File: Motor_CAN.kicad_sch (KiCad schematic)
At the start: 18 parts, among them J19 CAN_OUT, J20 MotorCANConnector, J27 CAN_TP, U14 ADM3055E, U15 CDSOT23-T24CAN

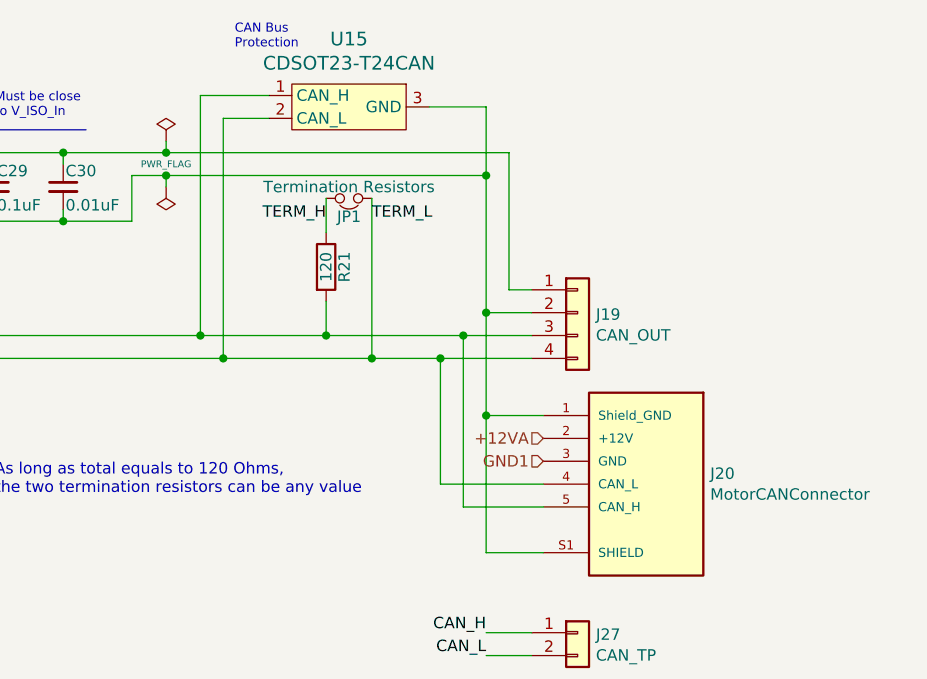
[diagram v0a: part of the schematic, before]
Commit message: Remove 12V isolator, swap CAN connector pins, etc.
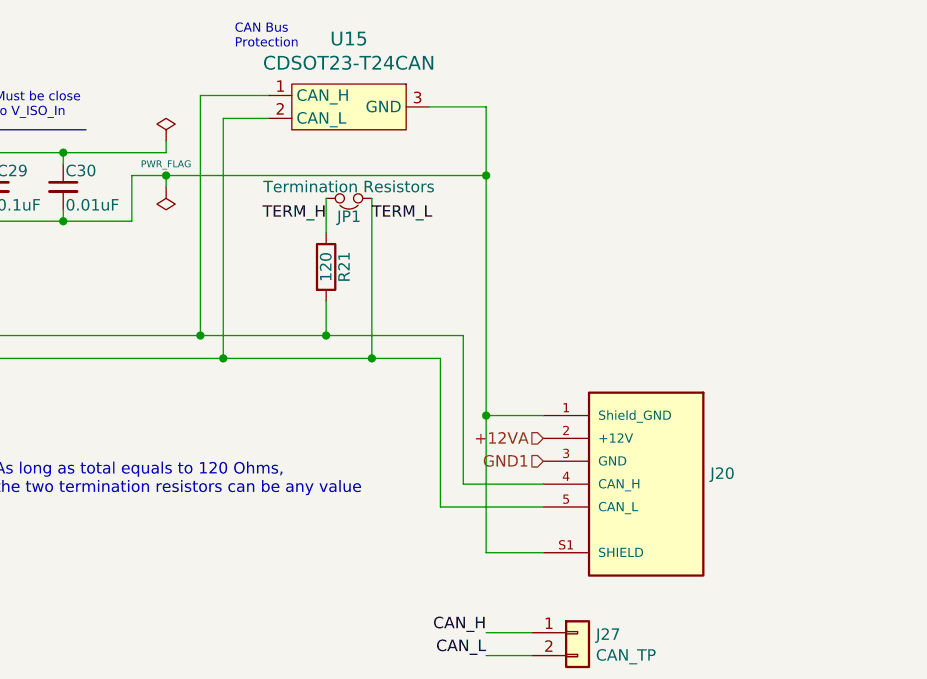
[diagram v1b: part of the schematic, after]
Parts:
- removed J19: CAN_OUT, UTSVT_Connectors:Molex_MicroFit3.0_1x4xP3.00mm_PolarizingPeg_Vertical, symbol Connector_Generic:Conn_01x04
- J20: value MotorCANConnector -> (none); symbol Dashboard-rescue:MotorCANConnector-utsvt-connectors -> Dashboard:MotorCANConnector-utsvt-connectors
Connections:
- net CAN_H: now also J20.4 (CAN_H); no longer J20.5 (CAN_H)
- net CAN_L: now also J20.5 (CAN_L); no longer J20.4 (CAN_L)

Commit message: Release v2.4 and gerbers
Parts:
- J20: value (none) -> MotorCANConnector
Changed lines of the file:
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@@
       (effects (font (size 1.27 1.27)) (justify right))
     )
-    (property "Value" "" (id 1) (at 244.602 119.253 0)
+    (property "Value" "MotorCANConnector" (id 1) (at 244.602 119.253 0)
       (effects (font (size 1.27 1.27)) (justify right))
     )

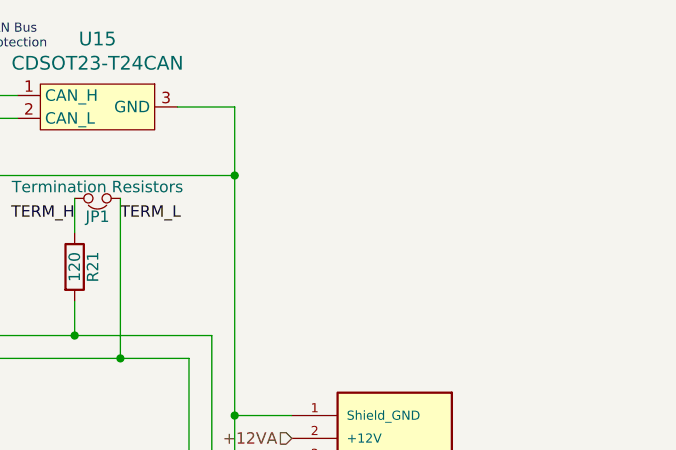
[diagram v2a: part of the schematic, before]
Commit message: Schematic notations for rework changes
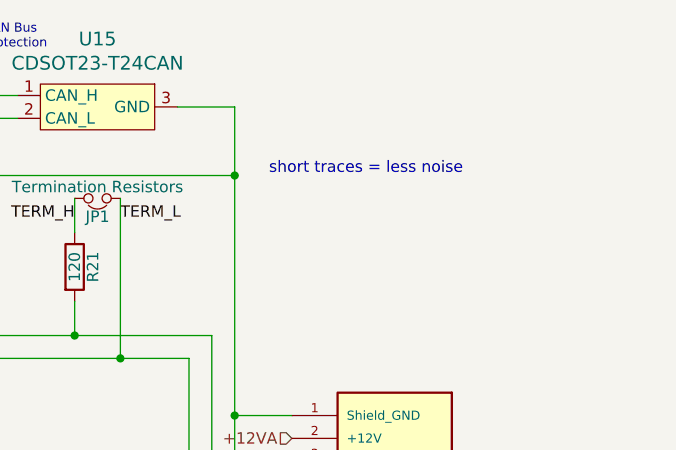
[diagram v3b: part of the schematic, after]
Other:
- note added: "short traces = less noise"

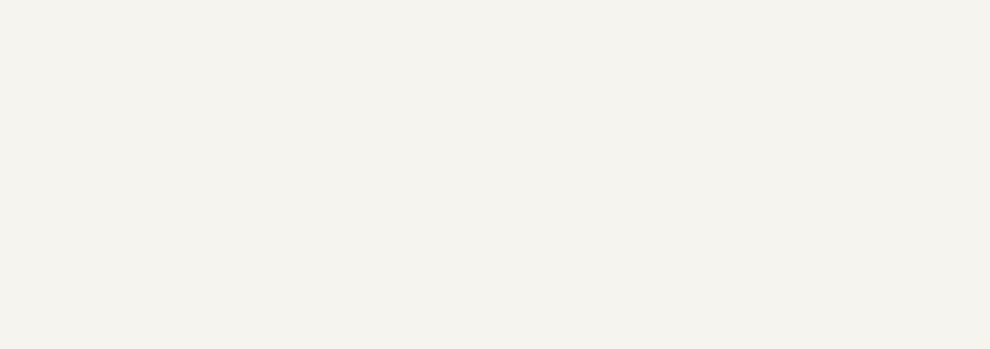
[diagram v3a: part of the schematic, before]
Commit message: Updated schematic in accordance to previous weeks annotated changes
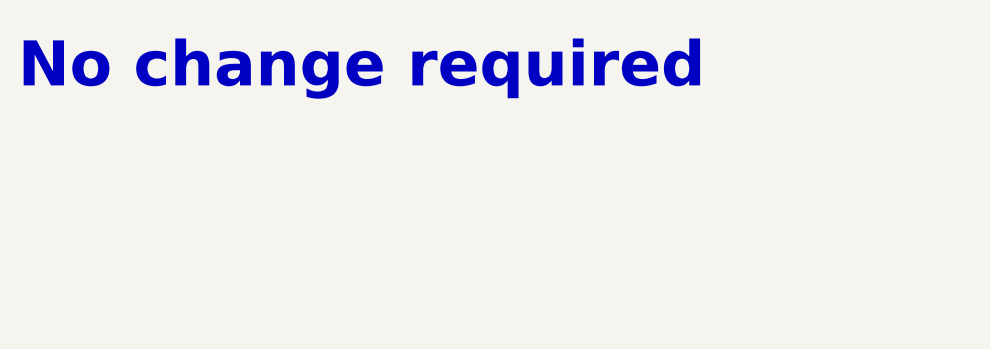
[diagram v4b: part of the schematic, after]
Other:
- note added: "No change required"
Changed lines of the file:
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@@
     (effects (font (size 1.27 1.27)) (justify left bottom))
+  )
+  (text "No change required\n" (at 15.24 22.86 0)
+    (effects (font (face "KiCad Font") (size 5 5) (thickness 1) bold (color 255 2 13 1)) (justify left bottom))
   )
   (text "CAN Bus\nProtection" (at 191.77 69.85 0)

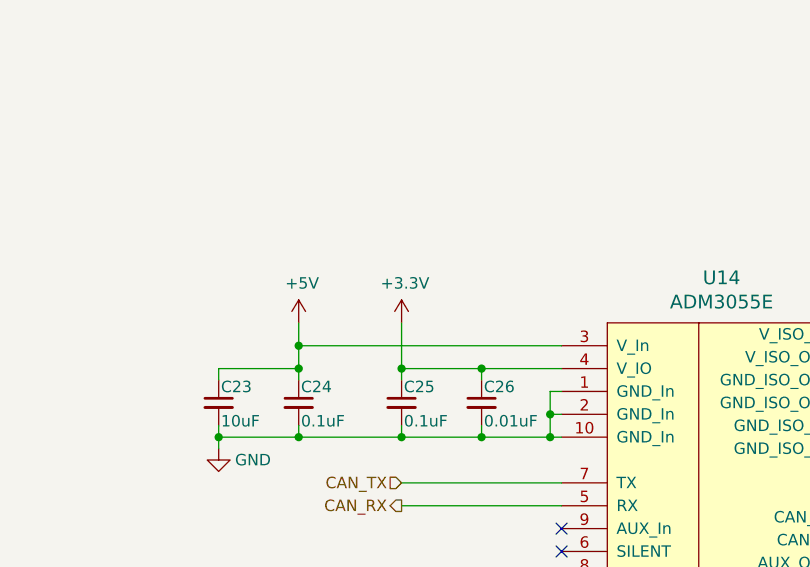
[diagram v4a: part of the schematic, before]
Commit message: Renamed Clk to PA5, removed CAN_TX/RX test points, deleted other .lck file and #auto_saved_files# (hopefully this does not break anything.
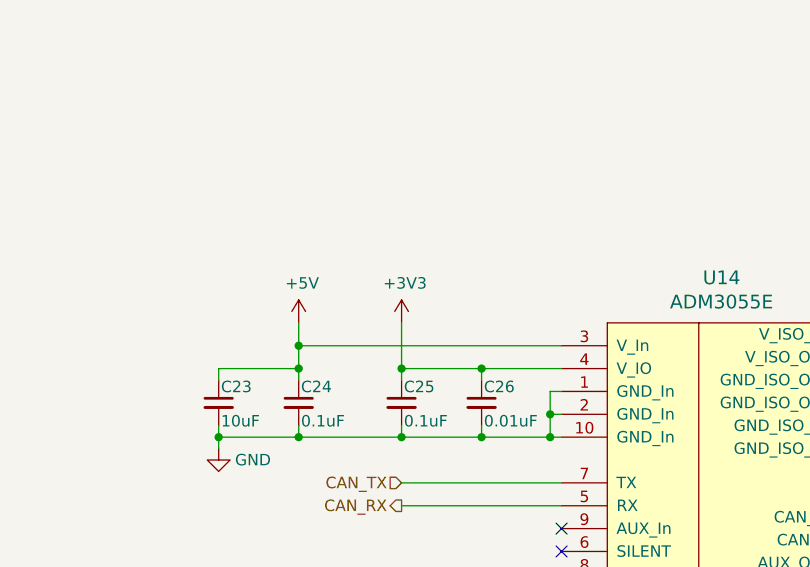
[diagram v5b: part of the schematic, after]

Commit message: Schematic finished :) hopefully not broken
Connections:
- net +12VA renamed +12V
- net GND1 renamed GNDPWR
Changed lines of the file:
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@@
 		)
 	)
-	(hierarchical_label "+12VA"
+	(hierarchical_label "+12V"
 		(shape input)
 		(at 226.06 113.03 180)
@@
 		)
 	)
-	(hierarchical_label "GND1"
+	(hierarchical_label "GNDPWR"
 		(shape input)
 		(at 226.06 115.57 180)

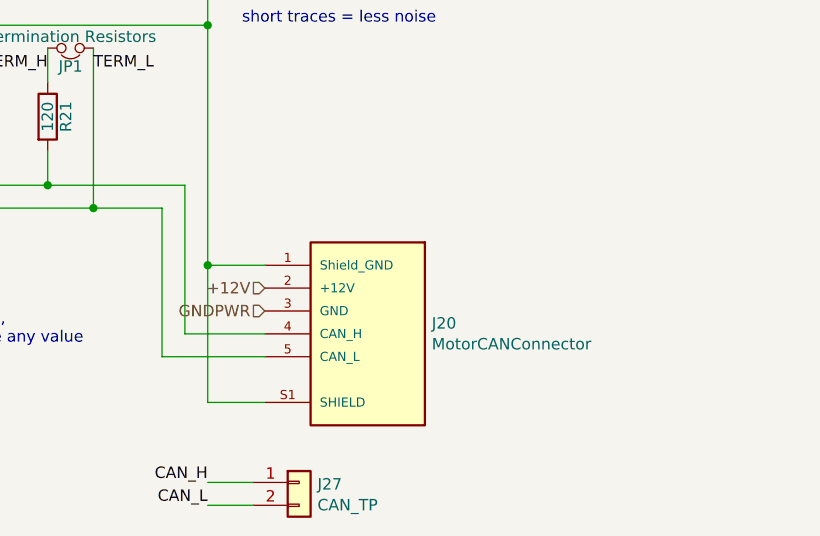
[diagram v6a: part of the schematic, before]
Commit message: Fuse added for motorCAN 12V
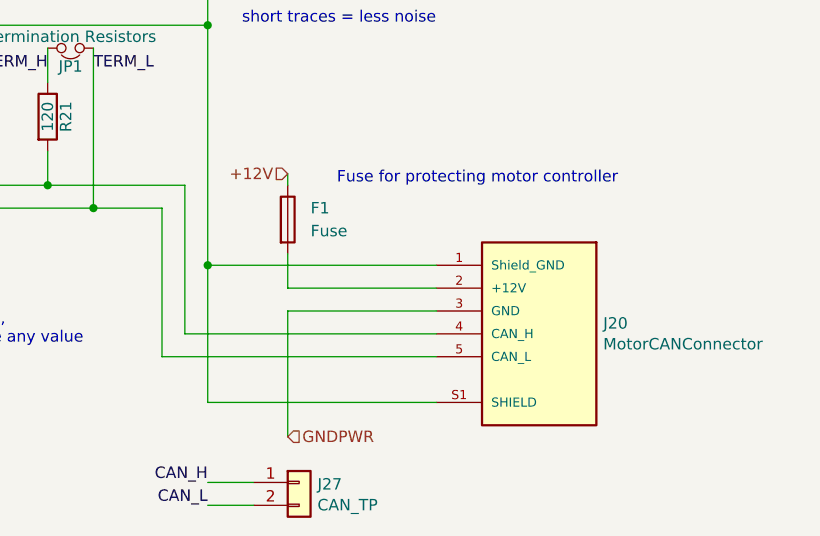
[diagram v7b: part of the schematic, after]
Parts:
- added F1: Fuse, symbol Device:Fuse
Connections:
- net +12V: now also F1.1; no longer J20.2 (+12V)
- new net: F1.2, J20.2 (+12V)
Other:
- note added: "Fuse for protecting motor controller"
- moved on the sheet: J20
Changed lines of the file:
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@@
 	(wire
 		(pts
-			(xy 219.71 110.49) (xy 226.06 110.49)
+			(xy 228.6 115.57) (xy 245.11 115.57)
+		)
+		(stroke
+			(width 0)
+			(type default)
+		)
+	)
+	(wire
+		(pts
+			(xy 219.71 110.49) (xy 245.11 110.49)
 		)
 		(stroke
@@
 	(wire
 		(pts
-			(xy 219.71 125.73) (xy 226.06 125.73)
+			(xy 219.71 125.73) (xy 245.11 125.73)
 		)
 		(stroke
@@
 	(wire
 		(pts
+			(xy 228.6 109.22) (xy 228.6 113.03)
+		)
+		(stroke
+			(width 0)
+			(type default)
+		)
+	)
+	(wire
+		(pts
 			(xy 187.96 74.93) (xy 187.96 101.6)
 		)
@@
 	(wire
 		(pts
-			(xy 217.17 118.11) (xy 226.06 118.11)
+			(xy 217.17 118.11) (xy 245.11 118.11)
 		)
 		(stroke
@@
 	(wire
 		(pts
+			(xy 228.6 101.6) (xy 228.6 100.33)
+		)
+		(stroke
+			(width 0)
+			(type default)
+		)
+	)
+	(wire
+		(pts
 			(xy 53.34 85.09) (xy 62.23 85.09)
 		)
@@
 	(wire
 		(pts
+			(xy 228.6 129.54) (xy 228.6 115.57)
+		)
+		(stroke
+			(width 0)
+			(type default)
+		)
+	)
+	(wire
+		(pts
 			(xy 195.58 74.93) (xy 187.96 74.93)
 		)
@@
 	(wire
 		(pts
+			(xy 228.6 113.03) (xy 245.11 113.03)
+		)
+		(stroke
+			(width 0)
+			(type default)
+		)
+	)
+	(wire
+		(pts
 			(xy 219.71 110.49) (xy 219.71 125.73)
 		)
@@
 	(wire
 		(pts
-			(xy 214.63 120.65) (xy 226.06 120.65)
+			(xy 214.63 120.65) (xy 245.11 120.65)
 		)
 		(stroke
@@
 		)
 	)
+	(text "Fuse for protecting motor controller\n"
+		(exclude_from_sim no)
+		(at 249.682 100.838 0)
+		(effects
+			(font
+				(size 1.27 1.27)
+				(color 255 0 2 1)
+			)
+		)
+	)
 	(text "CAN Bus\nProtection"
 		(exclude_from_sim no)
@@
 	(hierarchical_label "+12V"
 		(shape input)
-		(at 226.06 113.03 180)
+		(at 228.6 100.33 180)
 		(fields_autoplaced yes)
 		(effects
@@
 	(hierarchical_label "GNDPWR"
 		(shape input)
-		(at 226.06 115.57 180)
+		(at 228.6 129.54 0)
 		(fields_autoplaced yes)
 		(effects
@@
 				(size 1.27 1.27)
 			)
-			(justify right)
+			(justify left)
 		)
 	)
@@
 	(symbol
 		(lib_id "Dashboard:MotorCANConnector-utsvt-connectors")
-		(at 233.68 130.81 0)
+		(at 252.73 130.81 0)
 		(mirror y)
 		(unit 1)
@@
 		(dnp no)
 		(property "Reference" "J20"
-			(at 244.602 116.9416 0)
+			(at 263.652 116.9416 0)
 			(effects
 				(font
@@
 		)
 		(property "Value" "MotorCANConnector"
-			(at 244.602 119.253 0)
+			(at 263.652 119.253 0)
 			(effects
 				(font
@@
 		)
 		(property "Footprint" "UTSVT_Connectors:TE_4-2172079-2"
-			(at 233.68 130.81 0)
+			(at 252.73 130.81 0)
 			(effects
 				(font
@@
 		)
 		(property "Datasheet" ""
-			(at 233.68 130.81 0)
+			(at 252.73 130.81 0)
 			(effects
 				(font
@@
 		)
 		(property "Description" ""
-			(at 233.68 130.81 0)
+			(at 252.73 130.81 0)
 			(effects
 				(font
@@
 		)
 		(property "Digikey" "https://www.digikey.com/product-detail/en/te-connectivity-amp-connectors/4-2172079-2/A120861-ND/5118755"
-			(at 233.68 130.81 0)
+			(at 252.73 130.81 0)
 			(effects
 				(font
@@
 					(unit 1)
 				)
+			)
+		)
+	)
+	(symbol
+		(lib_id "Device:Fuse")
+		(at 228.6 105.41 0)
+		(unit 1)
+		(exclude_from_sim no)
+		(in_bom yes)
+		(on_board yes)
+		(dnp no)
+		(fields_autoplaced yes)
+		(property "Reference" "F1"
+			(at 231.14 104.1399 0)
+			(effects
+				(font
+					(size 1.27 1.27)
+				)
+				(justify left)
+			)
+		)
+		(property "Value" "Fuse"
+			(at 231.14 106.6799 0)
+			(effects
+				(font
+					(size 1.27 1.27)
+				)
+				(justify left)
+			)
+		)
+		(property "Footprint" ""
+			(at 226.822 105.41 90)
+			(effects
+				(font
+					(size 1.27 1.27)
+				)
+				(hide yes)
+			)
+		)
+		(property "Datasheet" "~"
+			(at 228.6 105.41 0)
+			(effects
+				(font
+					(size 1.27 1.27)
+				)
+				(hide yes)
+			)
+		)
+		(property "Description" "Fuse"
+			(at 228.6 105.41 0)
+			(effects
+				(font
+					(size 1.27 1.27)
+				)
+				(hide yes)
+			)
+		)
+		(pin "2"
+		)
+		(pin "1"
+		)
+		(instances
+			(project ""
+				(path "/66218487-e316-4467-9eba-79d4626ab24e/00000000-0000-0000-0000-00005f6018fb"
+					(reference "F1")
+					(unit 1)
+				)

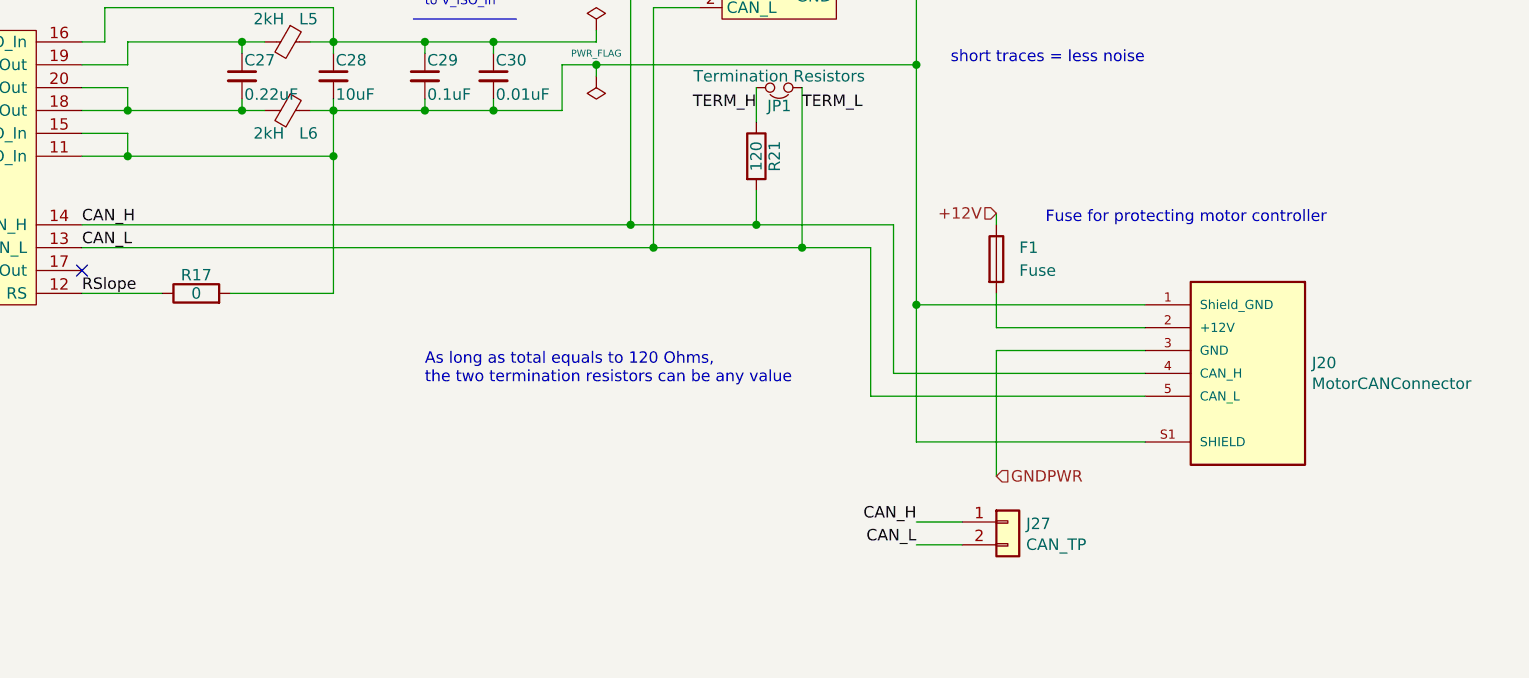
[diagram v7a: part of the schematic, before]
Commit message: Flipped optoisolators, changed resistor values, added second connector to motor can and disconnected shield pins for now since I haven't seen them used (will chack against old version to see what the circuit looked like), copied power-in circuit from contactor board, added optoisolator to timer and blinker light connection.
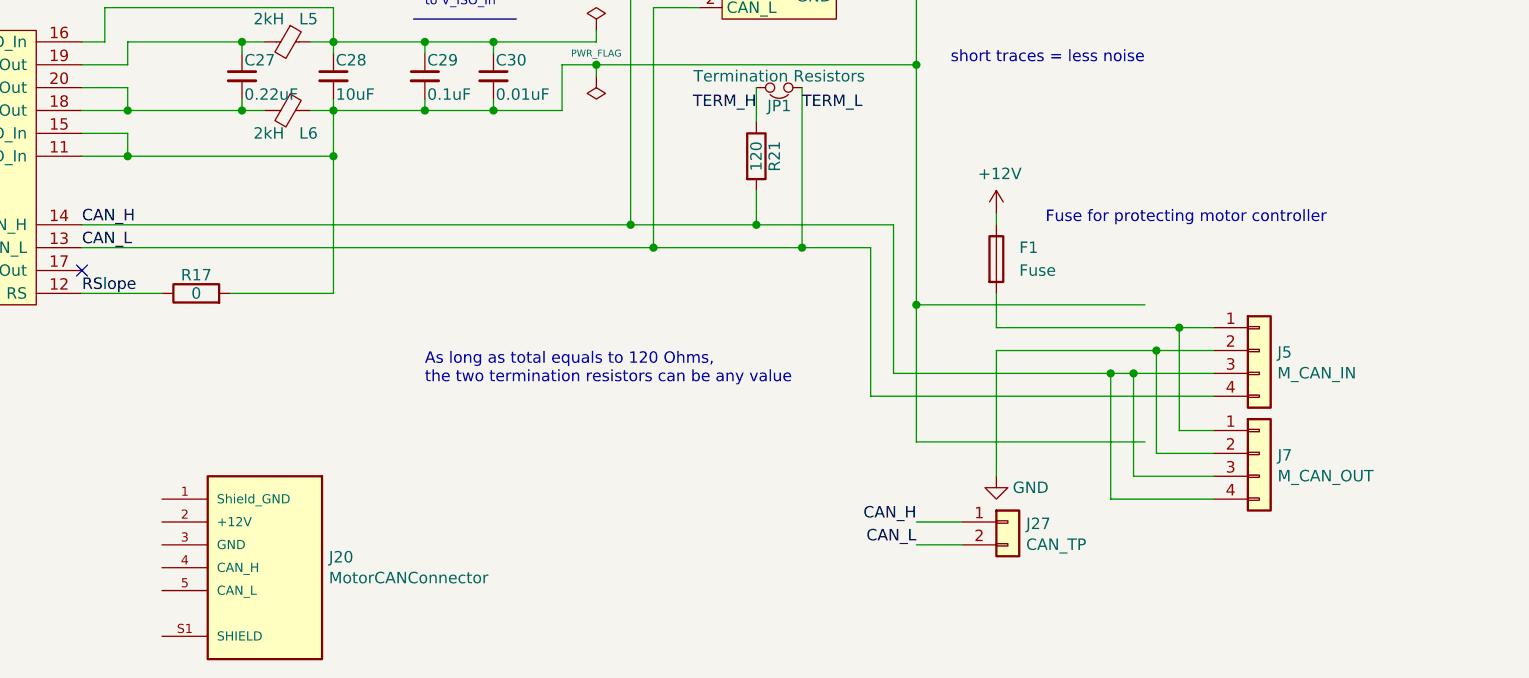
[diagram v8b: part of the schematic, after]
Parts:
- added J5: M_CAN_IN, UTSVT_Connectors:Molex_MicroFit3.0_1x4xP3.00mm_PolarizingPeg_Vertical, symbol Connector_Generic:Conn_01x04
- added J7: M_CAN_OUT, UTSVT_Connectors:Molex_MicroFit3.0_1x4xP3.00mm_PolarizingPeg_Vertical, symbol Connector_Generic:Conn_01x04
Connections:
- net CAN_H: now also J5.3 (Pin_3), J7.3 (Pin_3), J7.4 (Pin_4); no longer J20.4 (CAN_H)
- net CAN_L: now also J5.4 (Pin_4); no longer J20.5 (CAN_L)
- net GND: now also J5.2 (Pin_2), J7.2 (Pin_2)
- net at C28.2, C29.2, C30.2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: no longer J20.1 (Shield_GND), J20.S1 (SHIELD)
- net at J20.2 (+12V): no longer F1.2
- net GNDPWR: no longer names the net of J20.3 (GND)
- new net: F1.2, J5.1 (Pin_1), J7.1 (Pin_1)
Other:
- moved on the sheet: J20
